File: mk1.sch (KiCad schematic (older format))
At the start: 22 parts, among them J1 USB, P1 BUS 1, P2 BUS 2, P3 BUS 3, P5 ICP SEL, SW1 RESET, U1 WD65C02, U2 AT28C256, U3 CY7C199, U4 74HC132, U5 MXO45HS

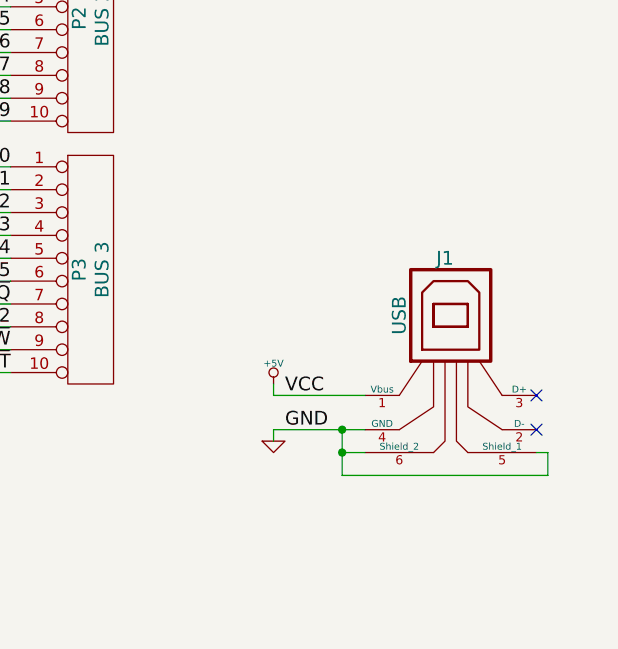
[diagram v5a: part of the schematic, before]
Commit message: add 7805 regulator
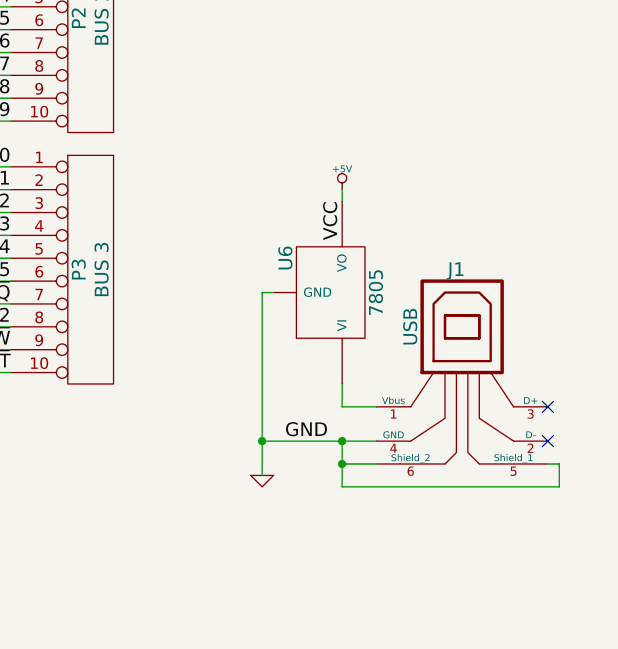
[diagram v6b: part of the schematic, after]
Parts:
- added U6: 7805, symbol 7805
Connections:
- net +5V: now also U6.VO; no longer J1.1 (Vbus)
- net GND: now also U6.GND
- new net: J1.1 (Vbus), U6.VI
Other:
- moved on the sheet: J1
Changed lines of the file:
@@
 $EndComp
 $Comp
-L GND #PWR01
+L GND #PWR3
 U 1 1 54770ACA
 P 2400 3700
-F 0 "#PWR01" H 2400 3700 30  0001 C CNN
+F 0 "#PWR3" H 2400 3700 30  0001 C CNN
 F 1 "GND" H 2400 3630 30  0001 C CNN
 F 2 "" H 2400 3700 60  0000 C CNN
@@
 $EndComp
 $Comp
-L GND #PWR02
+L GND #PWR7
 U 1 1 54770BB7
 P 4600 3700
-F 0 "#PWR02" H 4600 3700 30  0001 C CNN
+F 0 "#PWR7" H 4600 3700 30  0001 C CNN
 F 1 "GND" H 4600 3630 30  0001 C CNN
 F 2 "" H 4600 3700 60  0000 C CNN
@@
 $EndComp
 $Comp
-L GND #PWR03
+L GND #PWR12
 U 1 1 54770C0F
 P 6850 3700
-F 0 "#PWR03" H 6850 3700 30  0001 C CNN
+F 0 "#PWR12" H 6850 3700 30  0001 C CNN
 F 1 "GND" H 6850 3630 30  0001 C CNN
 F 2 "" H 6850 3700 60  0000 C CNN
@@
 $EndComp
 $Comp
-L +5V #PWR04
+L +5V #PWR11
 U 1 1 54770C6A
 P 6850 1650
-F 0 "#PWR04" H 6850 1740 20  0001 C CNN
+F 0 "#PWR11" H 6850 1740 20  0001 C CNN
 F 1 "+5V" H 6850 1740 30  0000 C CNN
 F 2 "" H 6850 1650 60  0000 C CNN
@@
 $EndComp
 $Comp
-L +5V #PWR05
+L +5V #PWR6
 U 1 1 54770CCB
 P 4600 1650
-F 0 "#PWR05" H 4600 1740 20  0001 C CNN
+F 0 "#PWR6" H 4600 1740 20  0001 C CNN
 F 1 "+5V" H 4600 1740 30  0000 C CNN
 F 2 "" H 4600 1650 60  0000 C CNN
@@
 $EndComp
 $Comp
-L +5V #PWR06
+L +5V #PWR17
 U 1 1 54771541
 P 8200 1100
-F 0 "#PWR06" H 8200 1190 20  0001 C CNN
+F 0 "#PWR17" H 8200 1190 20  0001 C CNN
 F 1 "+5V" H 8200 1190 30  0000 C CNN
 F 2 "" H 8200 1100 60  0000 C CNN
@@
 $EndComp
 $Comp
-L +5V #PWR07
+L +5V #PWR2
 U 1 1 54771900
 P 2400 1650
-F 0 "#PWR07" H 2400 1740 20  0001 C CNN
+F 0 "#PWR2" H 2400 1740 20  0001 C CNN
 F 1 "+5V" H 2400 1740 30  0000 C CNN
 F 2 "" H 2400 1650 60  0000 C CNN
@@
 	7950 3050 8050 2950
 $Comp
-L +5V #PWR08
+L +5V #PWR1
 U 1 1 54770EF9
 P 750 2650
-F 0 "#PWR08" H 750 2740 20  0001 C CNN
+F 0 "#PWR1" H 750 2740 20  0001 C CNN
 F 1 "+5V" H 750 2740 30  0000 C CNN
 F 2 "" H 750 2650 60  0000 C CNN
@@
 ~RST
 $Comp
-L +5V #PWR09
+L +5V #PWR4
 U 1 1 54775AB8
 P 2900 5700
-F 0 "#PWR09" H 2900 5790 20  0001 C CNN
+F 0 "#PWR4" H 2900 5790 20  0001 C CNN
 F 1 "+5V" H 2900 5790 30  0000 C CNN
 F 2 "" H 2900 5700 60  0000 C CNN
@@
 $EndComp
 $Comp
-L GND #PWR010
+L GND #PWR5
 U 1 1 54775ABE
 P 2900 7400
-F 0 "#PWR010" H 2900 7400 30  0001 C CNN
+F 0 "#PWR5" H 2900 7400 30  0001 C CNN
 F 1 "GND" H 2900 7330 30  0001 C CNN
 F 2 "" H 2900 7400 60  0000 C CNN
@@
 $EndComp
 $Comp
-L +5V #PWR011
+L +5V #PWR20
 U 1 1 54776FF2
 P 9600 6550
-F 0 "#PWR011" H 9600 6640 20  0001 C CNN
+F 0 "#PWR20" H 9600 6640 20  0001 C CNN
 F 1 "+5V" H 9600 6640 30  0000 C CNN
 F 2 "" H 9600 6550 60  0000 C CNN
@@
 $EndComp
 $Comp
-L GND #PWR012
+L GND #PWR21
 U 1 1 54776FF8
 P 9600 7050
-F 0 "#PWR012" H 9600 7050 30  0001 C CNN
+F 0 "#PWR21" H 9600 7050 30  0001 C CNN
 F 1 "GND" H 9600 6980 30  0001 C CNN
 F 2 "" H 9600 7050 60  0000 C CNN
@@
 AT U1\n
 $Comp
-L +5V #PWR013
+L +5V #PWR25
 U 1 1 54777152
 P 10000 6550
-F 0 "#PWR013" H 10000 6640 20  0001 C CNN
+F 0 "#PWR25" H 10000 6640 20  0001 C CNN
 F 1 "+5V" H 10000 6640 30  0000 C CNN
 F 2 "" H 10000 6550 60  0000 C CNN
@@
 $EndComp
 $Comp
-L GND #PWR014
+L GND #PWR26
 U 1 1 54777158
 P 10000 7050
-F 0 "#PWR014" H 10000 7050 30  0001 C CNN
+F 0 "#PWR26" H 10000 7050 30  0001 C CNN
 F 1 "GND" H 10000 6980 30  0001 C CNN
 F 2 "" H 10000 7050 60  0000 C CNN
@@
 AT U2\n
 $Comp
-L +5V #PWR015
+L +5V #PWR27
 U 1 1 54777165
 P 10400 6550
-F 0 "#PWR015" H 10400 6640 20  0001 C CNN
+F 0 "#PWR27" H 10400 6640 20  0001 C CNN
 F 1 "+5V" H 10400 6640 30  0000 C CNN
 F 2 "" H 10400 6550 60  0000 C CNN
@@
 $EndComp
 $Comp
-L GND #PWR016
+L GND #PWR28
 U 1 1 5477716B
 P 10400 7050
-F 0 "#PWR016" H 10400 7050 30  0001 C CNN
+F 0 "#PWR28" H 10400 7050 30  0001 C CNN
 F 1 "GND" H 10400 6980 30  0001 C CNN
 F 2 "" H 10400 7050 60  0000 C CNN
@@
 L USB J1
 U 1 1 54777AA5
-P 10350 4150
-F 0 "J1" H 10300 4550 60  0000 C CNN
-F 1 "USB" V 10100 4300 60  0000 C CNN
-F 2 "" H 10350 4150 60  0000 C CNN
-F 3 "" H 10350 4150 60  0000 C CNN
-	1    10350 4150
-	1    0    0    -1
-$EndComp
-NoConn ~ 10700 4500
-NoConn ~ 10700 4350
-$Comp
-L GND #PWR017
+P 10400 4200
+F 0 "J1" H 10350 4600 60  0000 C CNN
+F 1 "USB" V 10150 4350 60  0000 C CNN
+F 2 "" H 10400 4200 60  0000 C CNN
+F 3 "" H 10400 4200 60  0000 C CNN
+	1    10400 4200
+	1    0    0    -1
+$EndComp
+NoConn ~ 10750 4550
+NoConn ~ 10750 4400
+$Comp
+L GND #PWR19
 U 1 1 54777CF1
-P 9550 4550
-F 0 "#PWR017" H 9550 4550 30  0001 C CNN
-F 1 "GND" H 9550 4480 30  0001 C CNN
-F 2 "" H 9550 4550 60  0000 C CNN
-F 3 "" H 9550 4550 60  0000 C CNN
-	1    9550 4550
-	1    0    0    -1
-$EndComp
-$Comp
-L +5V #PWR018
+P 9500 4700
+F 0 "#PWR19" H 9500 4700 30  0001 C CNN
+F 1 "GND" H 9500 4630 30  0001 C CNN
+F 2 "" H 9500 4700 60  0000 C CNN
+F 3 "" H 9500 4700 60  0000 C CNN
+	1    9500 4700
+	1    0    0    -1
+$EndComp
+$Comp
+L +5V #PWR22
 U 1 1 54777CF7
-P 9550 4300
-F 0 "#PWR018" H 9550 4390 20  0001 C CNN
-F 1 "+5V" H 9550 4390 30  0000 C CNN
-F 2 "" H 9550 4300 60  0000 C CNN
-F 3 "" H 9550 4300 60  0000 C CNN
-	1    9550 4300
+P 9850 3450
+F 0 "#PWR22" H 9850 3540 20  0001 C CNN
+F 1 "+5V" H 9850 3540 30  0000 C CNN
+F 2 "" H 9850 3450 60  0000 C CNN
+F 3 "" H 9850 3450 60  0000 C CNN
+	1    9850 3450
 	1    0    0    -1
 $EndComp
@@
 A15
 $Comp
-L +5V #PWR019
+L +5V #PWR13
 U 1 1 54775CAD
 P 7050 5750
-F 0 "#PWR019" H 7050 5840 20  0001 C CNN
+F 0 "#PWR13" H 7050 5840 20  0001 C CNN
 F 1 "+5V" H 7050 5840 30  0000 C CNN
 F 2 "" H 7050 5750 60  0000 C CNN
@@
 $EndComp
 $Comp
-L GND #PWR020
+L GND #PWR14
 U 1 1 54775CB3
 P 7050 6250
-F 0 "#PWR020" H 7050 6250 30  0001 C CNN
+F 0 "#PWR14" H 7050 6250 30  0001 C CNN
 F 1 "GND" H 7050 6180 30  0001 C CNN
 F 2 "" H 7050 6250 60  0000 C CNN
@@
 ~RST
 $Comp
-L +5V #PWR021
+L +5V #PWR29
 U 1 1 547780EC
 P 10800 6550
-F 0 "#PWR021" H 10800 6640 20  0001 C CNN
+F 0 "#PWR29" H 10800 6640 20  0001 C CNN
 F 1 "+5V" H 10800 6640 30  0000 C CNN
 F 2 "" H 10800 6550 60  0000 C CNN
@@
 $EndComp
 $Comp
-L GND #PWR022
+L GND #PWR30
 U 1 1 547780F2
 P 10800 7050
-F 0 "#PWR022" H 10800 7050 30  0001 C CNN
+F 0 "#PWR30" H 10800 7050 30  0001 C CNN
 F 1 "GND" H 10800 6980 30  0001 C CNN
 F 2 "" H 10800 7050 60  0000 C CNN
@@
 PHI2
 $Comp
-L +5V #PWR023
+L +5V #PWR15
 U 1 1 5477A666
 P 7050 6550
-F 0 "#PWR023" H 7050 6640 20  0001 C CNN
+F 0 "#PWR15" H 7050 6640 20  0001 C CNN
 F 1 "+5V" H 7050 6640 30  0000 C CNN
 F 2 "" H 7050 6550 60  0000 C CNN
@@
 $EndComp
 $Comp
-L GND #PWR024
+L GND #PWR16
 U 1 1 5477A66C
 P 7050 7050
-F 0 "#PWR024" H 7050 7050 30  0001 C CNN
+F 0 "#PWR16" H 7050 7050 30  0001 C CNN
 F 1 "GND" H 7050 6980 30  0001 C CNN
 F 2 "" H 7050 7050 60  0000 C CNN
@@
 Text Label 8400 2050 2    60   ~ 0
 GND
-Text Label 9600 4500 0    60   ~ 0
+Text Label 9600 4550 0    60   ~ 0
 GND
-Text Label 9600 4350 0    60   ~ 0
+Text Label 9850 3500 3    60   ~ 0
 VCC
 Entry Bus Bus
@@
 	750  4050 850  3950
 $Comp
-L GND #PWR025
+L GND #PWR18
 U 1 1 5477159F
 P 8200 2100
-F 0 "#PWR025" H 8200 2100 30  0001 C CNN
+F 0 "#PWR18" H 8200 2100 30  0001 C CNN
 F 1 "GND" H 8200 2030 30  0001 C CNN
 F 2 "" H 8200 2100 60  0000 C CNN
@@
 $EndComp
 $Comp
-L +5V #PWR026
+L +5V #PWR23
 U 1 1 54778FC6
 P 10000 5700
-F 0 "#PWR026" H 10000 5790 20  0001 C CNN
+F 0 "#PWR23" H 10000 5790 20  0001 C CNN
 F 1 "+5V" H 10000 5790 30  0000 C CNN
 F 2 "" H 10000 5700 60  0000 C CNN
@@
 $EndComp
 $Comp
-L GND #PWR027
+L GND #PWR24
 U 1 1 54778FCC
 P 10000 6100
-F 0 "#PWR027" H 10000 6100 30  0001 C CNN
+F 0 "#PWR24" H 10000 6100 30  0001 C CNN
 F 1 "GND" H 10000 6030 30  0001 C CNN
 F 2 "" H 10000 6100 60  0000 C CNN
@@
 	3700 6500 3900 6500
 Wire Wire Line
-	9550 4500 9950 4500
-Wire Wire Line
-	9850 4500 9850 4700
-Wire Wire Line
-	9850 4600 9950 4600
-Wire Wire Line
-	9850 4700 10750 4700
-Wire Wire Line
-	10750 4700 10750 4600
-Wire Wire Line
-	10750 4600 10700 4600
-Connection ~ 9850 4600
-Wire Wire Line
-	9550 4500 9550 4550
-Connection ~ 9850 4500
-Wire Wire Line
-	9550 4300 9550 4350
-Wire Wire Line
-	9550 4350 9950 4350
+	9500 4550 10000 4550
+Wire Wire Line
+	9850 4550 9850 4750
+Wire Wire Line
+	9850 4650 10000 4650
+Wire Wire Line
+	9850 4750 10800 4750
+Wire Wire Line
+	10800 4750 10800 4650
+Wire Wire Line
+	10800 4650 10750 4650
+Connection ~ 9850 4650
+Connection ~ 9850 4550
+Wire Wire Line
+	9850 4400 10000 4400
 Wire Wire Line
 	7850 6000 8300 6000
@@
 A15
 $Comp
-L +5V #PWR028
+L +5V #PWR9
 U 1 1 5477FFE0
 P 5750 6450
-F 0 "#PWR028" H 5750 6540 20  0001 C CNN
+F 0 "#PWR9" H 5750 6540 20  0001 C CNN
 F 1 "+5V" H 5750 6540 30  0000 C CNN
 F 2 "" H 5750 6450 60  0000 C CNN
@@
 $EndComp
 $Comp
-L GND #PWR029
+L GND #PWR10
 U 1 1 5477FFE6
 P 5750 6950
-F 0 "#PWR029" H 5750 6950 30  0001 C CNN
+F 0 "#PWR10" H 5750 6950 30  0001 C CNN
 F 1 "GND" H 5750 6880 30  0001 C CNN
 F 2 "" H 5750 6950 60  0000 C CNN
@@
 	5300 6600 5350 6600
 $Comp
-L +5V #PWR030
+L +5V #PWR8
 U 1 1 54780058
 P 5300 6550
-F 0 "#PWR030" H 5300 6640 20  0001 C CNN
+F 0 "#PWR8" H 5300 6640 20  0001 C CNN
 F 1 "+5V" H 5300 6640 30  0000 C CNN
 F 2 "" H 5300 6550 60  0000 C CNN
@@
 	1    0    0    -1
 $EndComp
+$Comp
+L 7805 U6
+U 1 1 5477C5FE
+P 9800 3900
+F 0 "U6" H 9950 3704 60  0000 C CNN
+F 1 "7805" H 9800 4100 60  0000 C CNN
+F 2 "" H 9800 3900 60  0000 C CNN
+F 3 "" H 9800 3900 60  0000 C CNN
+	1    9800 3900
+	0    1    -1   0
+$EndComp
+Wire Wire Line
+	9850 3450 9850 3500
+Wire Wire Line
+	9850 4300 9850 4400
+Wire Wire Line
+	9500 3900 9500 4700
+Connection ~ 9500 4550
+Wire Wire Line
+	9500 3900 9550 3900
 $EndSCHEMATC

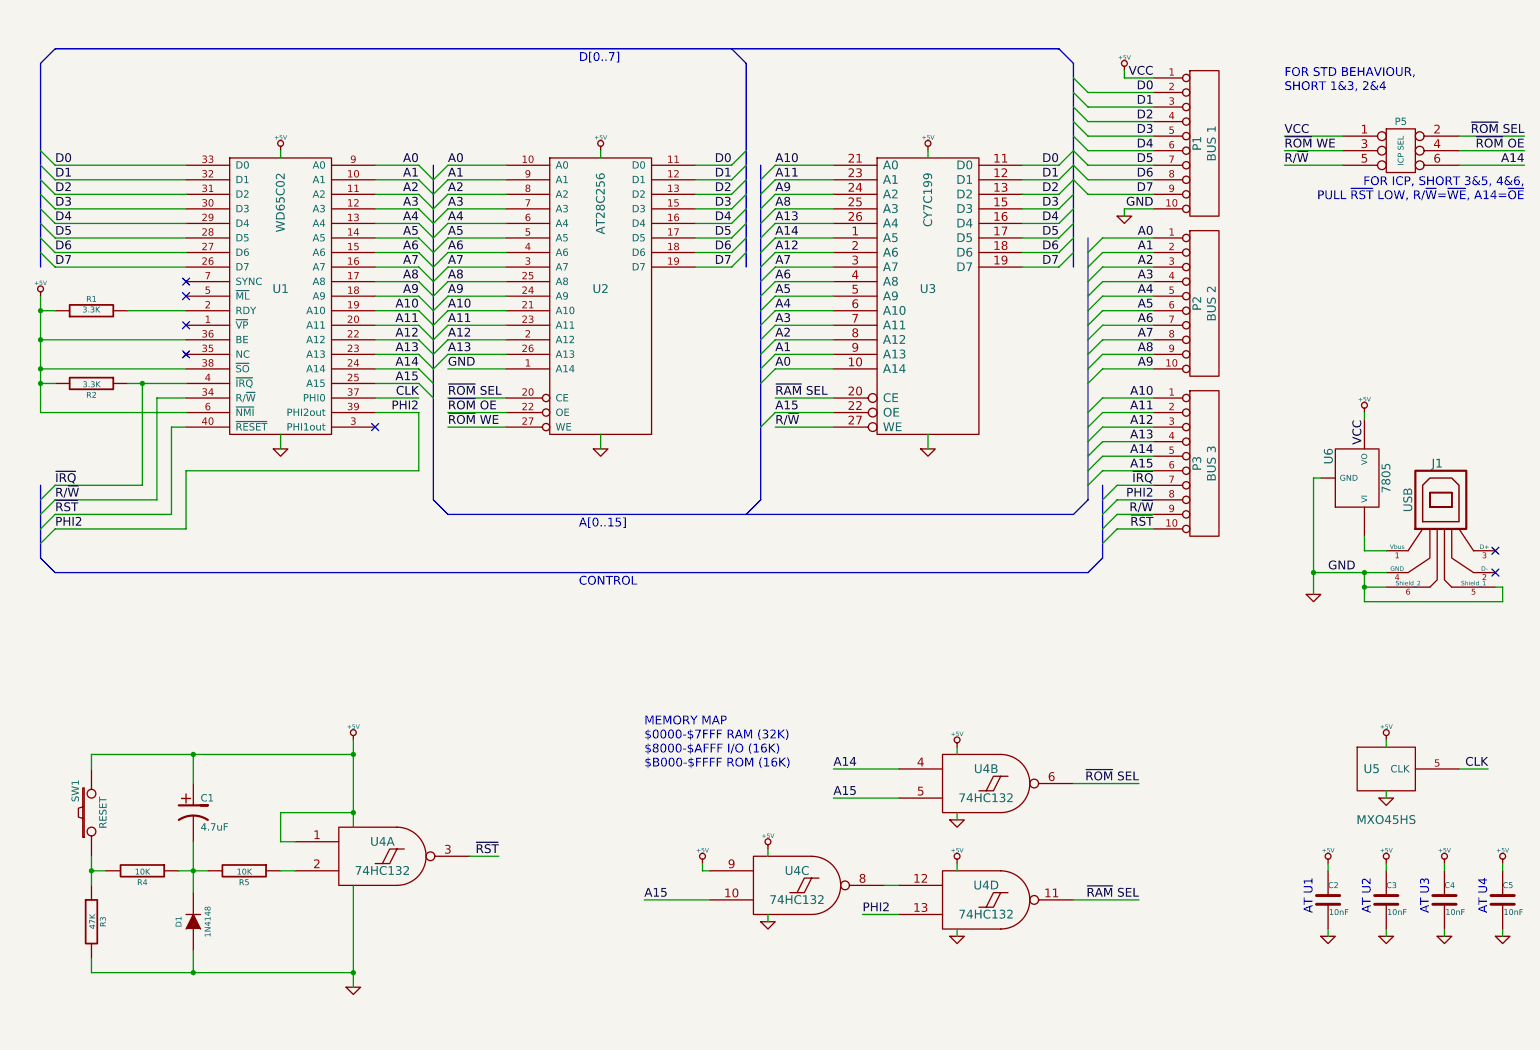
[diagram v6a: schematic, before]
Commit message: add capacitor across external bus VCC/GND
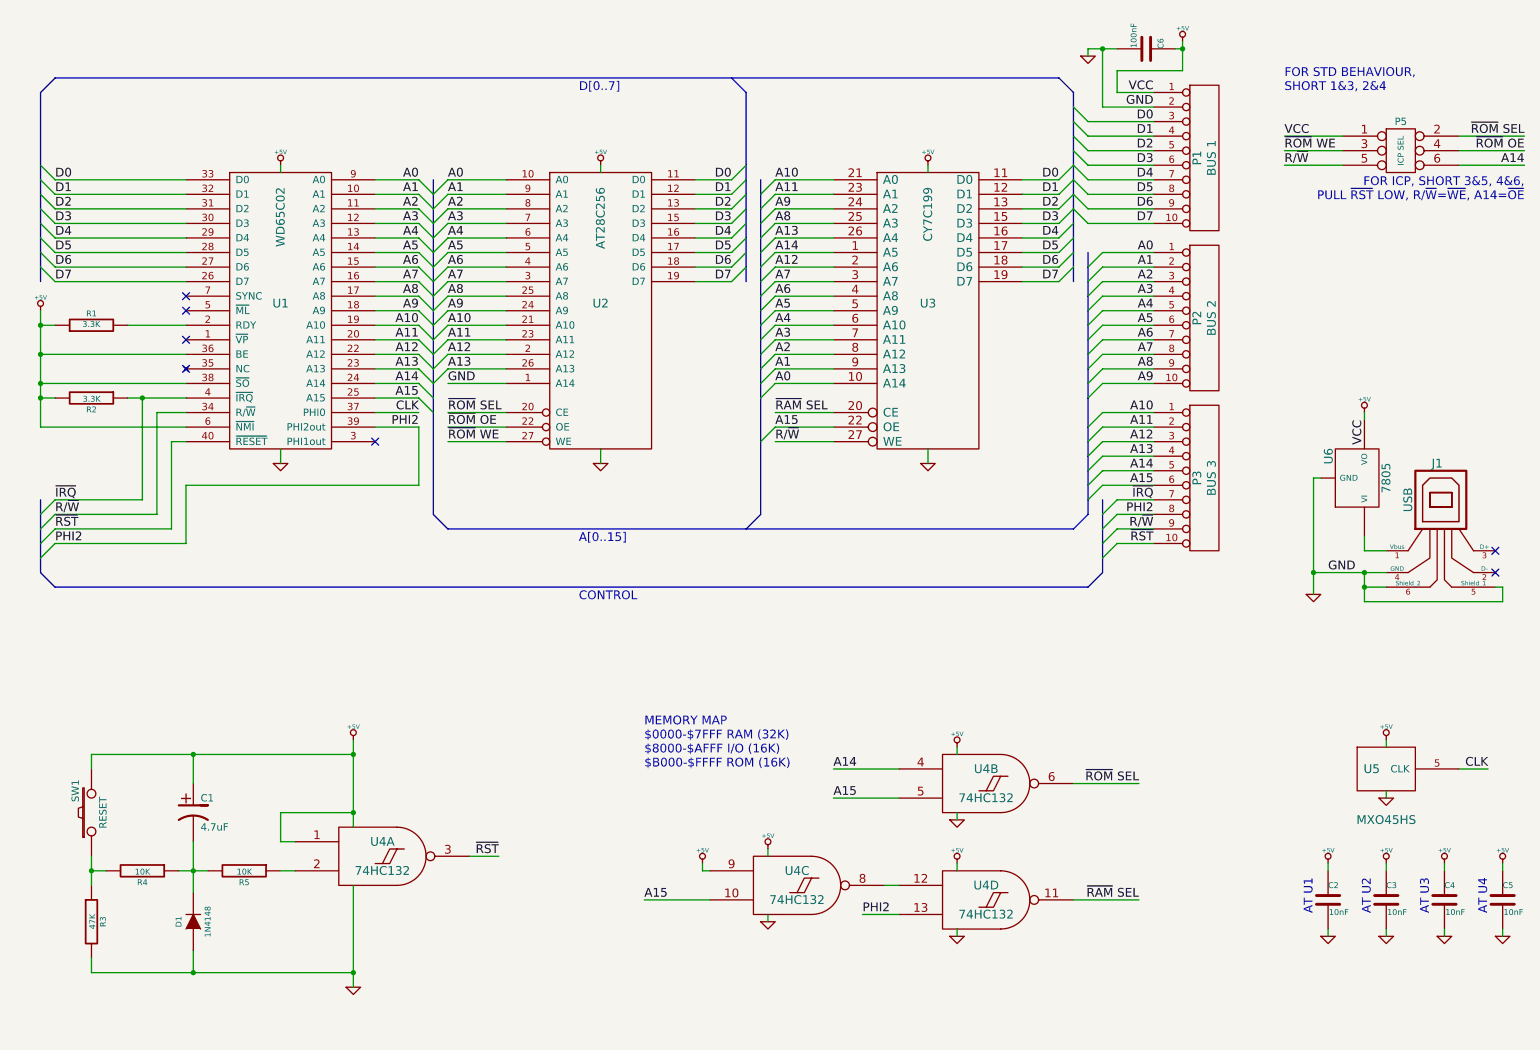
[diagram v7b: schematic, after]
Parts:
- added C6: 100nF, ~, symbol C
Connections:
- net +5V: now also C6.1
- net D0: now also P1.3 (P3); no longer P1.2 (P2)
- net D1: now also P1.4 (P4); no longer P1.3 (P3)
- net D2: now also P1.5 (P5); no longer P1.4 (P4)
- net D3: now also P1.6 (P6); no longer P1.5 (P5)
- net D4: now also P1.7 (P7); no longer P1.6 (P6)
- net D5: now also P1.8 (P8); no longer P1.7 (P7)
- net D6: now also P1.9 (P9); no longer P1.8 (P8)
- net D7: now also P1.10 (P10); no longer P1.9 (P9)
- net GND: now also P1.2 (P2), C6.2; no longer P1.10 (P10)
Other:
- moved on the sheet: P1, P2, P3, R1, R2, U1, U2, U3
